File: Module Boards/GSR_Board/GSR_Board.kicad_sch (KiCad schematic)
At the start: 0 parts

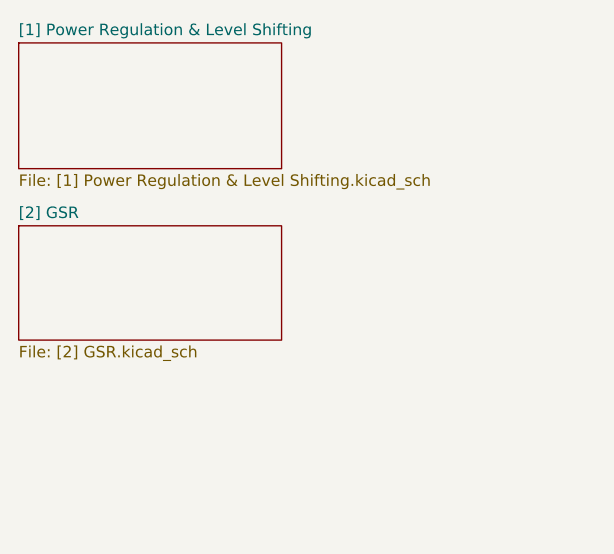
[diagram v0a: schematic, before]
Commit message: Added ADC to board and partially placed/routed the updated board
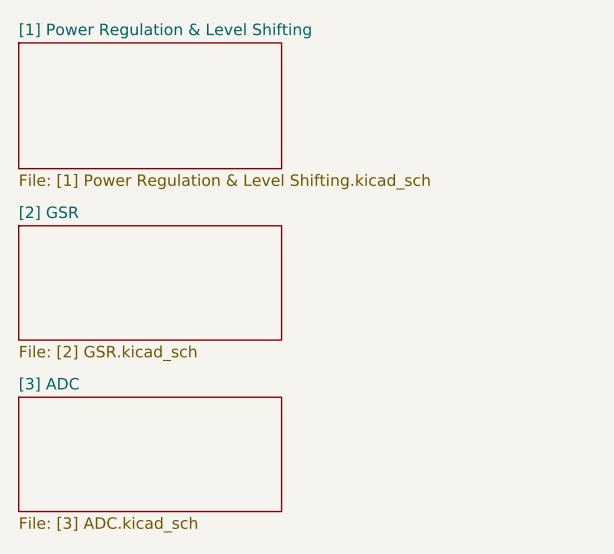
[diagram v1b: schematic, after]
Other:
- added sheet [3] ADC ([3] ADC.kicad_sch)
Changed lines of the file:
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@@
+		)
+	)
+	(sheet
+		(at 290.83 57.15)
+		(size 29.21 12.7)
+		(fields_autoplaced yes)
+		(stroke
+			(width 0.1524)
+			(type solid)
+		)
+		(fill
+			(color 0 0 0 0.0000)
+		)
+		(property "Sheetname" "[3] ADC"
+			(at 290.83 56.4384 0)
+			(effects
+				(font
+					(size 1.27 1.27)
+				)
+				(justify left bottom)
+			)
+		)
+		(property "Sheetfile" "[3] ADC.kicad_sch"
+			(at 290.83 70.4346 0)
+			(effects
+				(font
+					(size 1.27 1.27)
+				)
+				(justify left top)
+			)
+		)
+		(instances
+			(project "GSR_Board"
+				(path "/967fd416-113b-4abc-8322-5b19c6966929"
+					(page "4")
+				)
+			)
 		)
 	)
